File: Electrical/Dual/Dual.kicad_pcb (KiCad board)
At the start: 2 copper layers, 140 x 70 mm, 190 parts, among them J101 01x04, J102 02x04, J103 01x04, J104 01x03, J105 01x03, J106 01x03, J107 01x03, J108 01x03, J109 01x03, J110 01x04, J111 01x04, J112 01x04, J113 01x04, J114 01x03, J115 01x03, J116 01x03, J117 01x03, J201 01x03, J202 01x04, J203 01x03, J204 01x04, J205 01x03, J206 USB_OTG, J207 01x04, J208 01x02, J209 01x04, J210 01x02, J211 01x02, J212 4PostTerm, J213 2PostTerm, J214 2PostTerm, J215 2PostTerm, J216 2PostTerm, J217 2PostTerm, J218 01x02, J219 01x02, Q201 FDC6420C, Q202 FDG1024NZ, Q301 FDC6420C, Q401 FDC6420C, U201 TPD4S012, U202 ACS712ELCTR-05B-T, U203 ACS712ELCTR-05B-T, U204 24LC256, U205 LM2576HVS-ADJ, U206 LM2576HVS-ADJ, x100 02x05, x101 RoutaCell, x102 RoutaCell, x103 RoutaCell, x104 RoutaCell, x105 RoutaCell, x106 RoutaCell, x107 RoutaCell, x108 RoutaCell, x109 RoutaCell, x110 RoutaCell, x111 RoutaCell, x112 RoutaCell, x113 RoutaCell, x114 RoutaCell, x115 RoutaCell, x116 RoutaCell, x117 RoutaCell, x118 RoutaCell, x119 RoutaCell, x120 RoutaCell, x121 RoutaCell, x122 RoutaCell, x123 RoutaCell, x124 RoutaCell, x125 RoutaCell, x126 RoutaCell, x127 RoutaCell, x128 RoutaCell, x129 RoutaCell, x130 RoutaCell, x131 RoutaCell, x132 RoutaCell, x133 RoutaCell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

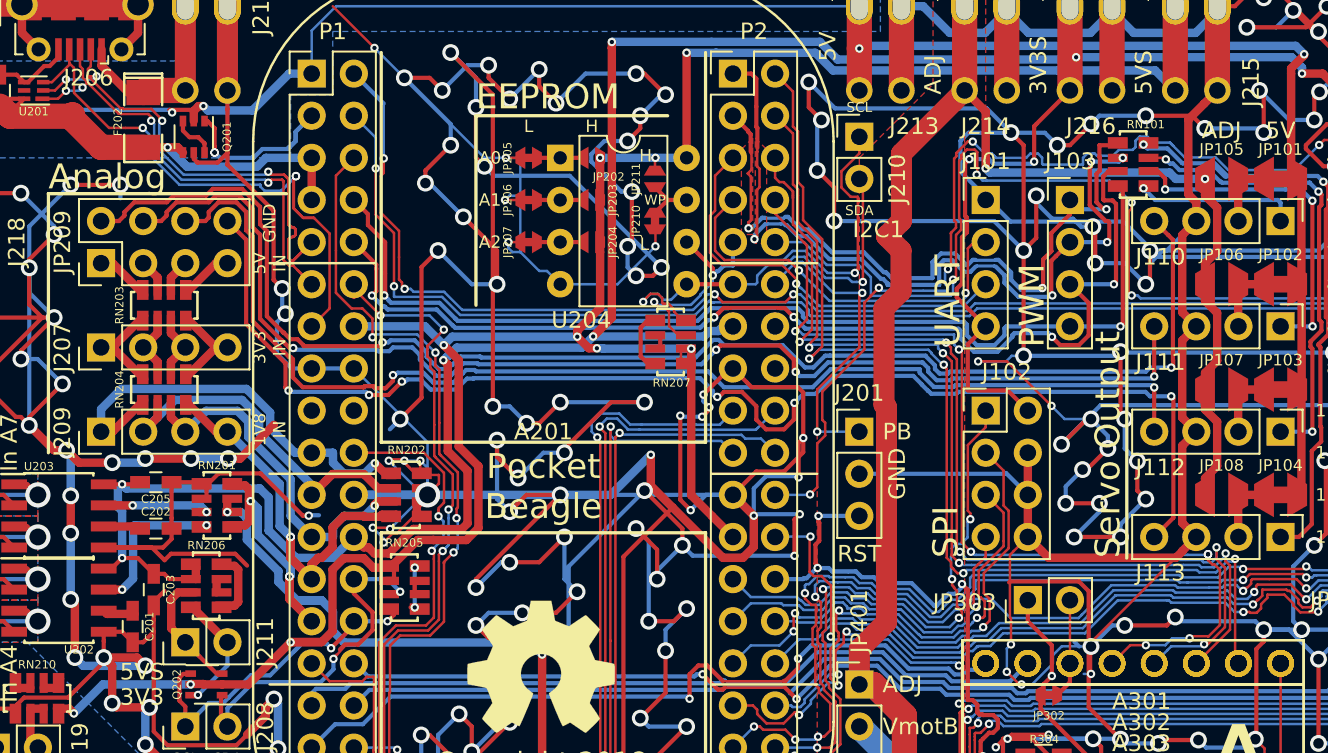
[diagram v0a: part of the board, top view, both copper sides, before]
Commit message: ACS712 -> ACS723
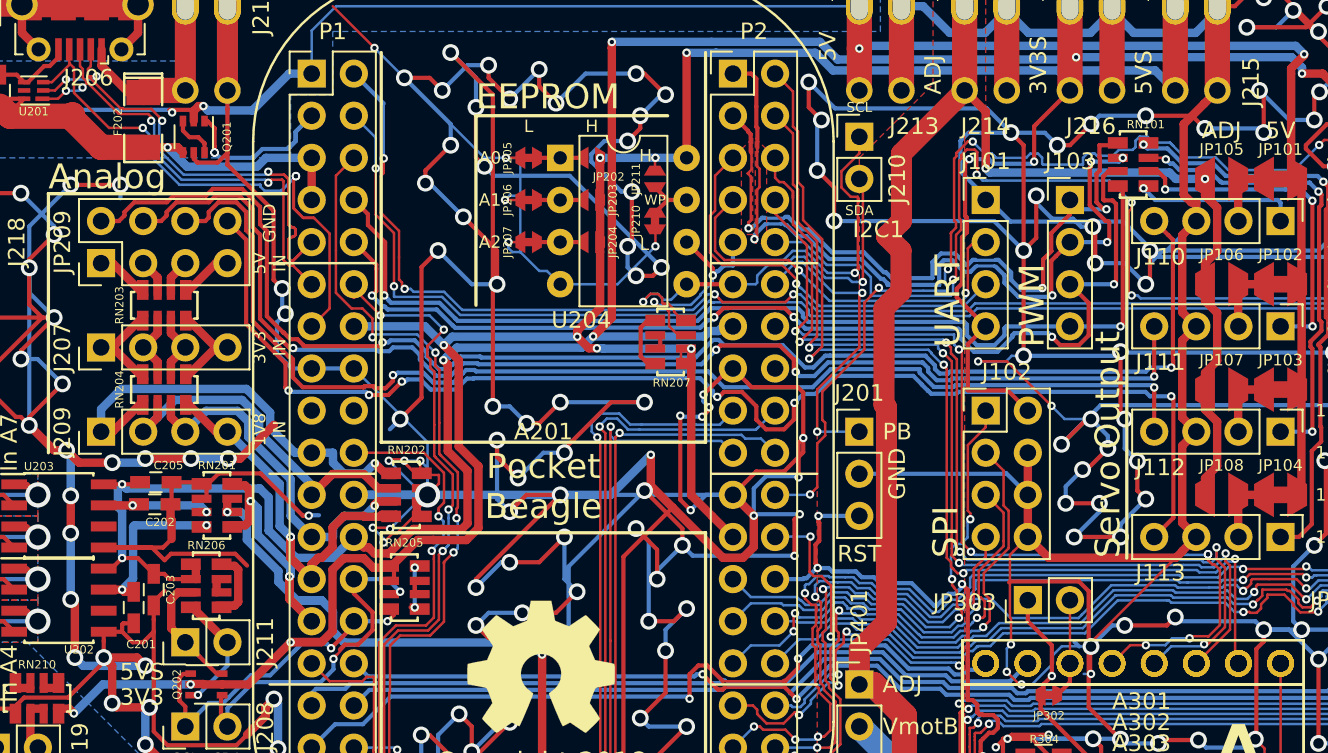
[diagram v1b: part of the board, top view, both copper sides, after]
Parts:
- U202, U203: value ACS712ELCTR-05B-T -> ACS723LLCTR-05AB-T
- moved C202 1.46 mm to (76.6, 96.8)
- moved C201 1.14 mm to (75.3, 103.0)
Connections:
- RN201 pad 7: Net-(RN201-Pad7) -> Net-(C202-Pad1)
- RN201 pad 8: Net-(RN201-Pad8) -> Net-(C201-Pad1)
- U202 pad 6: Net-(C201-Pad1) -> (no net)
- U202 pad 7: Net-(RN201-Pad8) -> Net-(C201-Pad1)
- U203 pad 6: Net-(C202-Pad1) -> (no net)
- U203 pad 7: Net-(RN201-Pad7) -> Net-(C202-Pad1)
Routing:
- net Net-(RN201-Pad8): track 9.64 -> 0.00 mm, vias 2 -> 0
- net Net-(C201-Pad1): track 1.95 -> 10.4 mm, vias 0 -> 2
- net Net-(RN201-Pad7): track 6.81 -> 0.00 mm, vias 2 -> 0
- net Net-(C202-Pad1): track 2.24 -> 7.22 mm, vias 0 -> 2
- net GND: track 2574.8 -> 2578.5 mm

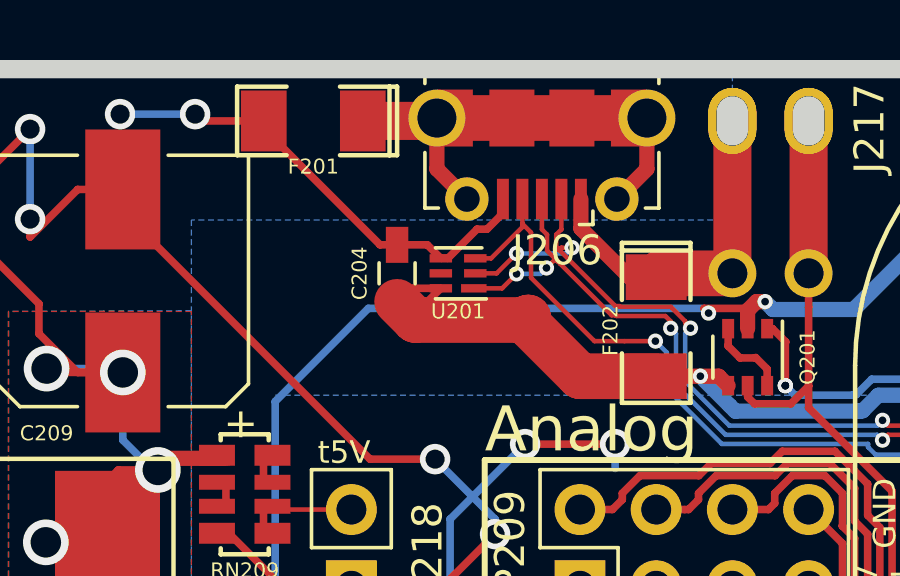
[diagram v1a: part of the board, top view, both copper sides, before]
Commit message: FB <> Fuse; FB == Ferrite Bead
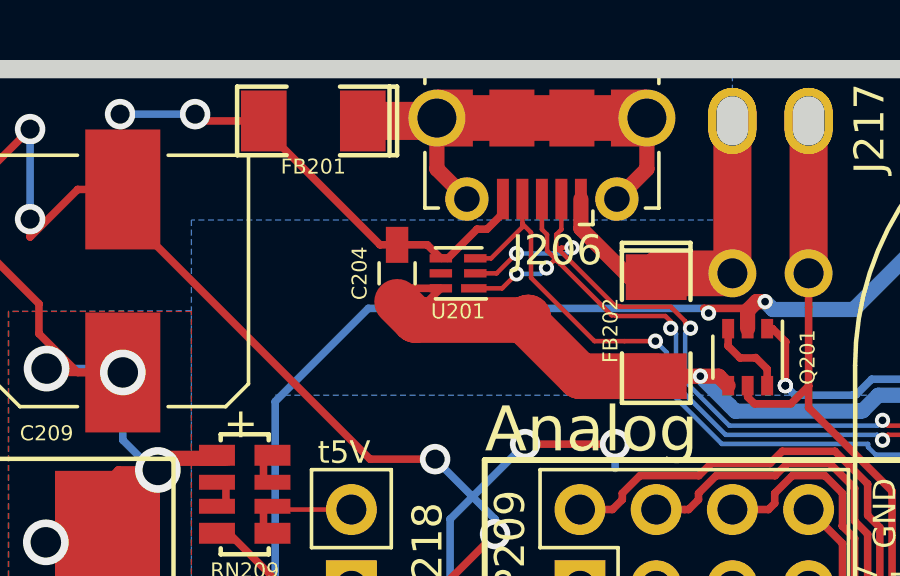
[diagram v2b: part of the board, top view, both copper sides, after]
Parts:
- FB201: renamed from F201; value Fuse -> 120
- FB202: renamed from F202; value Fuse -> 120

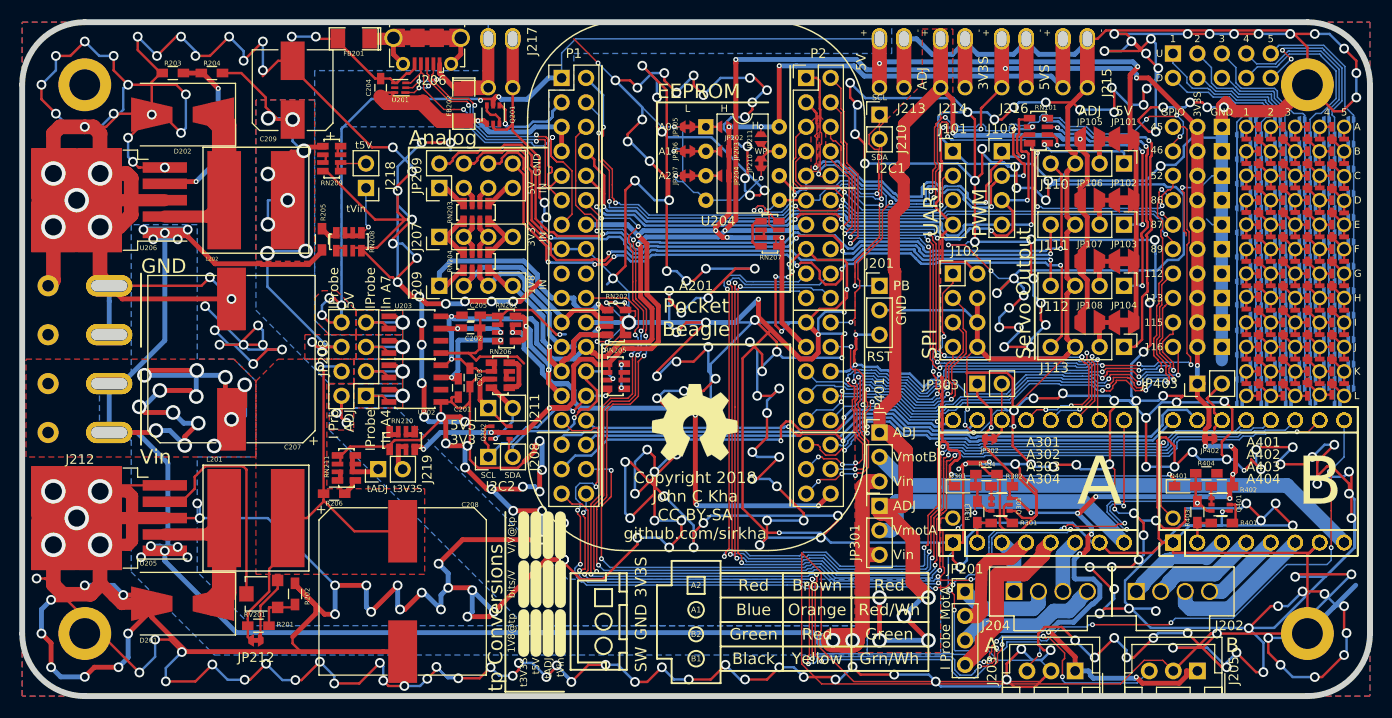
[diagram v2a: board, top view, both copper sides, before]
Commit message: Rearranged the power outputs to support TE Connectivity AMP connectors.
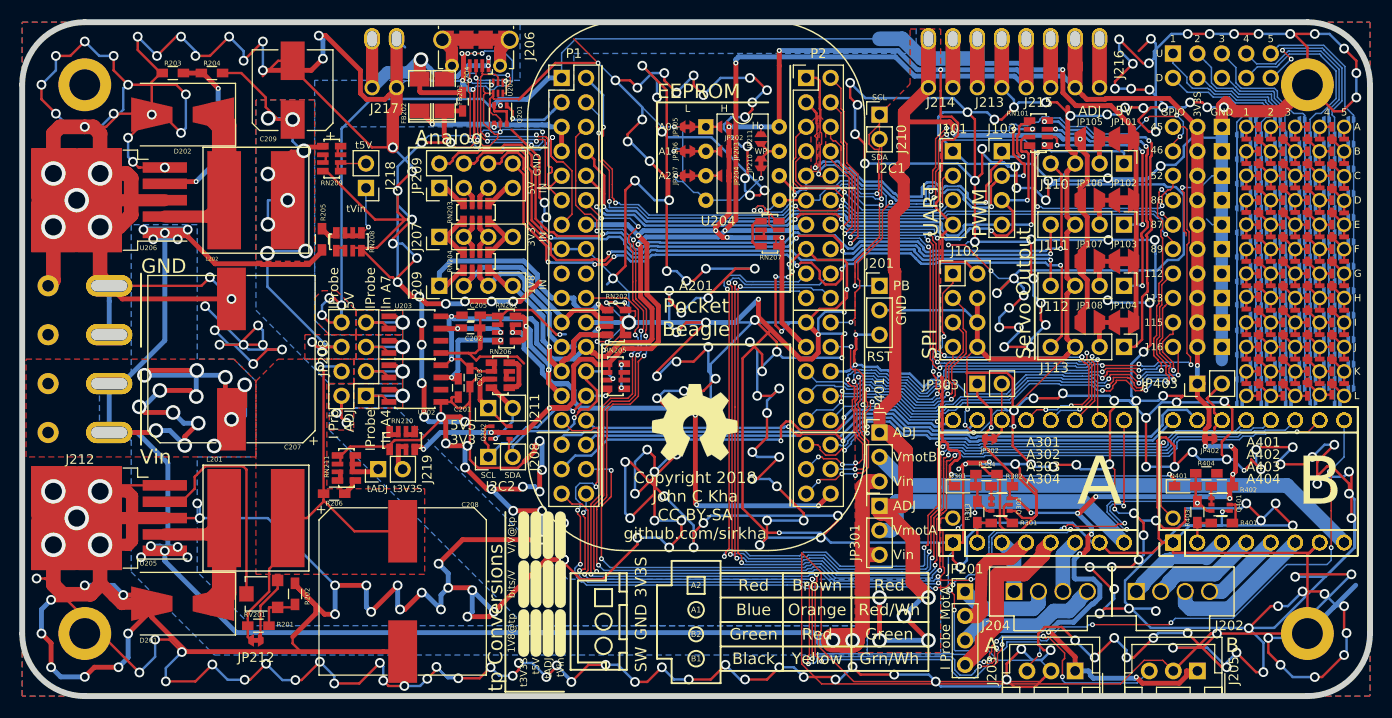
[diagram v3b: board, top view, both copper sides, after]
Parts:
- moved J217 12.1 mm to (67.6, 69.3)
- moved FB201 11.1 mm to (73.8, 72.6), turned to 90 degrees
- moved J213 10.2 mm to (130.5, 69.3)
- moved U201 10.2 mm to (79.4, 71.8), turned to 270 degrees
- moved C204 8.63 mm to (75.7, 73.3), turned to 270 degrees
- moved J216 7.62 mm to (140.6, 69.3)
- moved J206 5.08 mm to (77.1, 67.2)
- moved FB202 4.68 mm to (71.3, 72.6), turned to 90 degrees
- moved J215 3.81 mm to (135.6, 69.3)
- moved J214 1.27 mm to (125.4, 69.3)
- moved Q201 0.76 mm to (79.7, 74.6)
- moved RN101 0.25 mm to (135.6, 76.5)
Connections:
- C204 pad 1: /Common/usb1_vbus -> /Common/usb1_5V
- FB201 pad 1: Net-(FB201-Pad1) -> GND
- FB201 pad 2: GND -> Net-(FB201-Pad2)
- FB202 pad 1: /Common/usb1_5V -> /Common/usb1_vbus
- FB202 pad 2: /Common/usb1_vbus -> /Common/usb1_5V
- J206 pad 6: Net-(FB201-Pad1) -> Net-(FB201-Pad2)
- U201 pad 6: /Common/usb1_vbus -> /Common/usb1_5V
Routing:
- net GND: track 2578.5 -> 2651.5 mm, vias 371 -> 384
- net Net-(FB201-Pad1): track 22.1 -> 0.00 mm
- net /Common/usb1_5V: track 11.8 -> 33.4 mm, vias 0 -> 4
- net Net-(FB201-Pad2): track 0.00 -> 15.0 mm
- net /Common/usb1_vbus: track 27.3 -> 18.9 mm, vias 1 -> 2
- net /Common/usb1_d-: track 36.9 -> 31.9 mm, vias 4 -> 2
- net Vadj: track 137.4 -> 132.7 mm
- net 5VS: track 126.8 -> 123.2 mm
- net /Common/usb1_drvvbus: track 12.3 -> 8.86 mm, vias 2 -> 1
- net /gpio1_20: track 58.2 -> 55.4 mm
- net /gpio1_14: track 63.5 -> 60.8 mm
- net /Common/usb1_d+: track 29.4 -> 26.9 mm
- net /Common/usb1_id: track 37.3 -> 35.8 mm, vias 3 -> 5
- net +5V: track 150.3 -> 149.8 mm, vias 7 -> 5
- net 3V3S: track 322.6 -> 322.3 mm, vias 27 -> 24
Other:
- outline, holes or cut-outs redrawn

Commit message: Modified main power input footprint to support other connectors
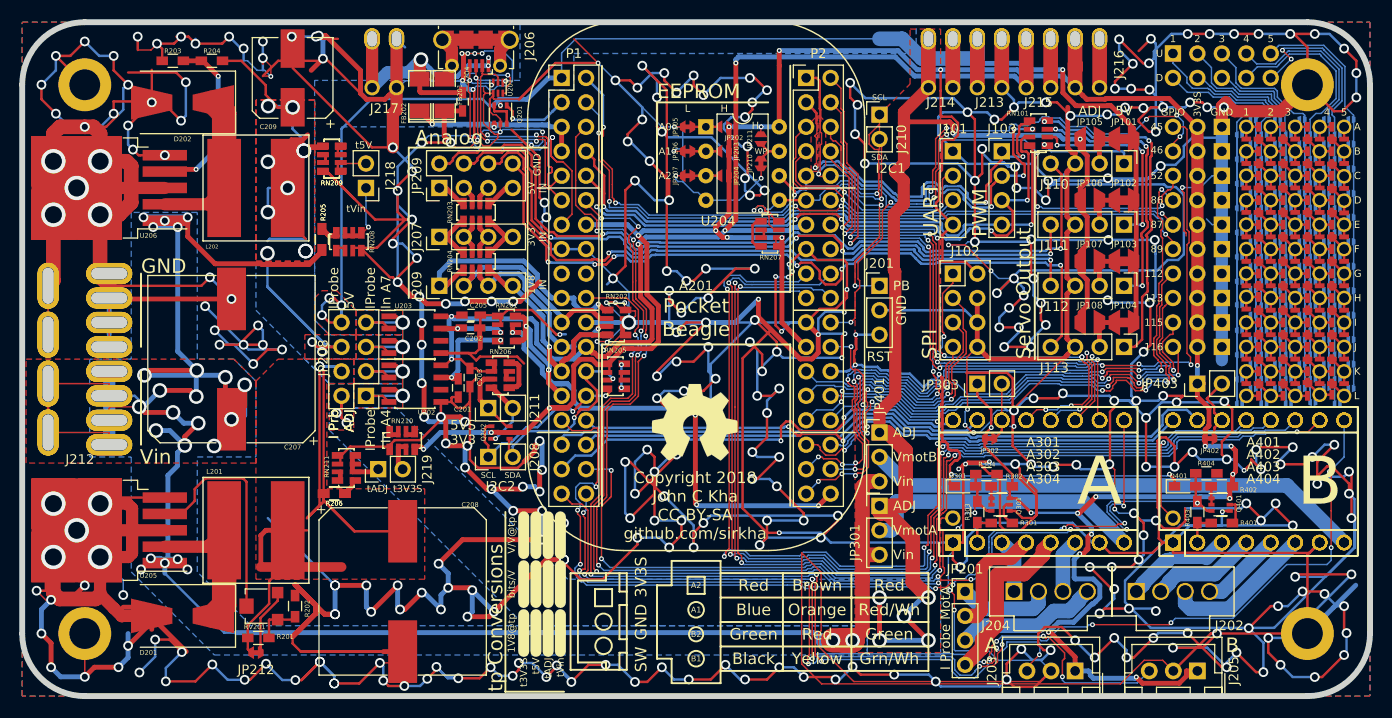
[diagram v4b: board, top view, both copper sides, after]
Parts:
- removed the R205 at (61.1, 87.6)
- removed the R206 at (62.4, 114.0)
- removed the RN209 at (62.2, 79.2)
- added R205 (x2): 12K, Resistors_SMD:R_0603_HandSoldering, F.Cu at (61.1, 87.6)
- added R206 (x2): 12K, Resistors_SMD:R_0603_HandSoldering, F.Cu at (62.4, 114.0)
- added RN209 (x2): 1K2, footprints:R_Array_1206x04, F.Cu at (62.2, 79.2)
- moved C209 1.27 mm to (58.1, 70.8)
- moved D201 1.27 mm to (46.7, 126.7)
- moved D202 1.27 mm to (46.7, 73.3)
- moved L201 1.27 mm to (54.3, 117.8)
- moved L202 1.27 mm to (54.3, 82.2)
- moved R202 1.27 mm to (58.3, 125.7)
- moved R203 1.27 mm to (45.6, 69.0)
- moved R204 1.27 mm to (49.7, 69.0)
- moved RV201 1.27 mm to (54.9, 125.7)
- moved U205 1.27 mm to (39.0, 117.8)
- moved U206 1.27 mm to (39.0, 82.2)
- moved JP212 1.27 mm to (54.3, 130.5)
- moved R201 1.27 mm to (54.5, 129.0)
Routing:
- net /Common/IP_vadj: track 45.2 -> 85.8 mm, vias 1 -> 2
- net Vin: track 246.5 -> 271.1 mm
- net GND: track 2651.5 -> 2668.6 mm, vias 384 -> 389
- net /Common/IP_5V: track 64.0 -> 70.9 mm
- net (no net): track 0.00 -> 4.06 mm, vias 0 -> 2
- net Net-(R205-Pad1): track 1.90 -> 3.79 mm
- net Net-(RN209-Pad2): track 0.80 -> 1.60 mm
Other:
- outline, holes or cut-outs redrawn

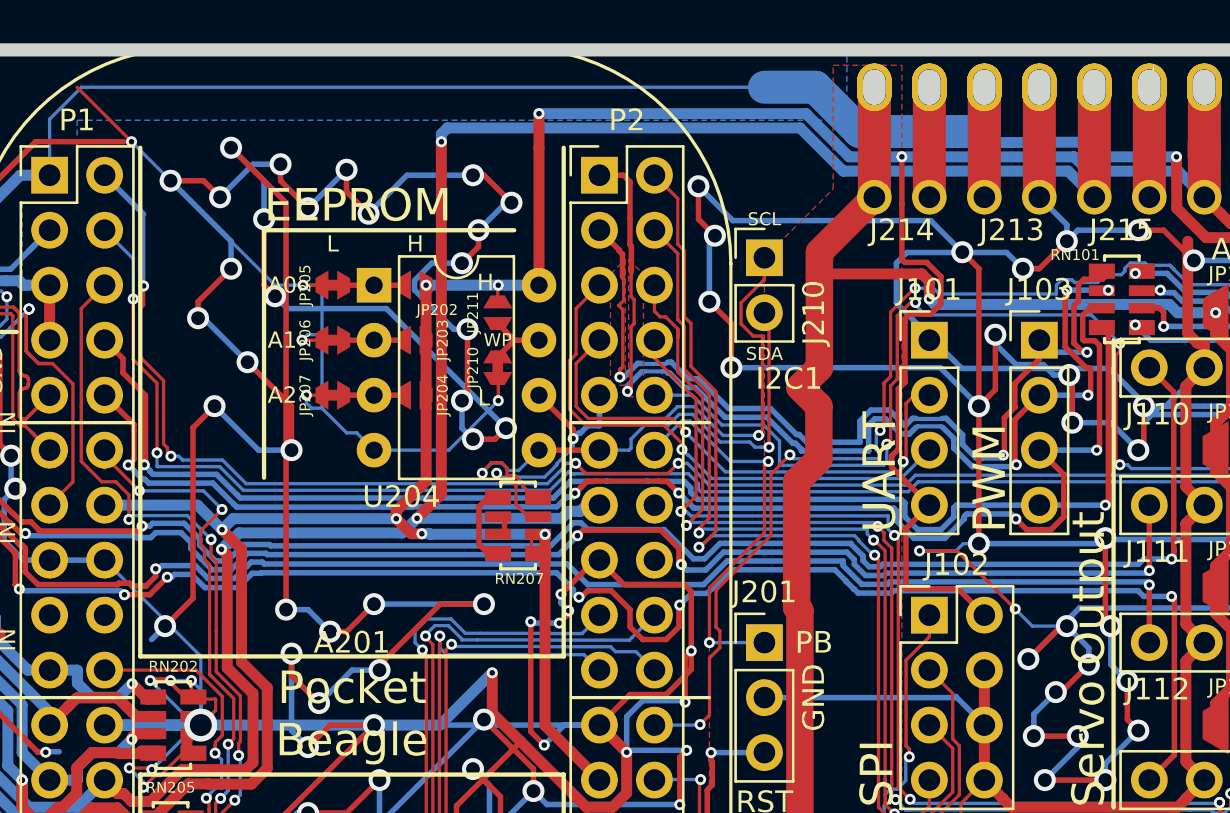
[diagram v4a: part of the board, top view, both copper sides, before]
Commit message: Rearranged EEPROM to add an MSOP option and make the address/WP pins more accessible
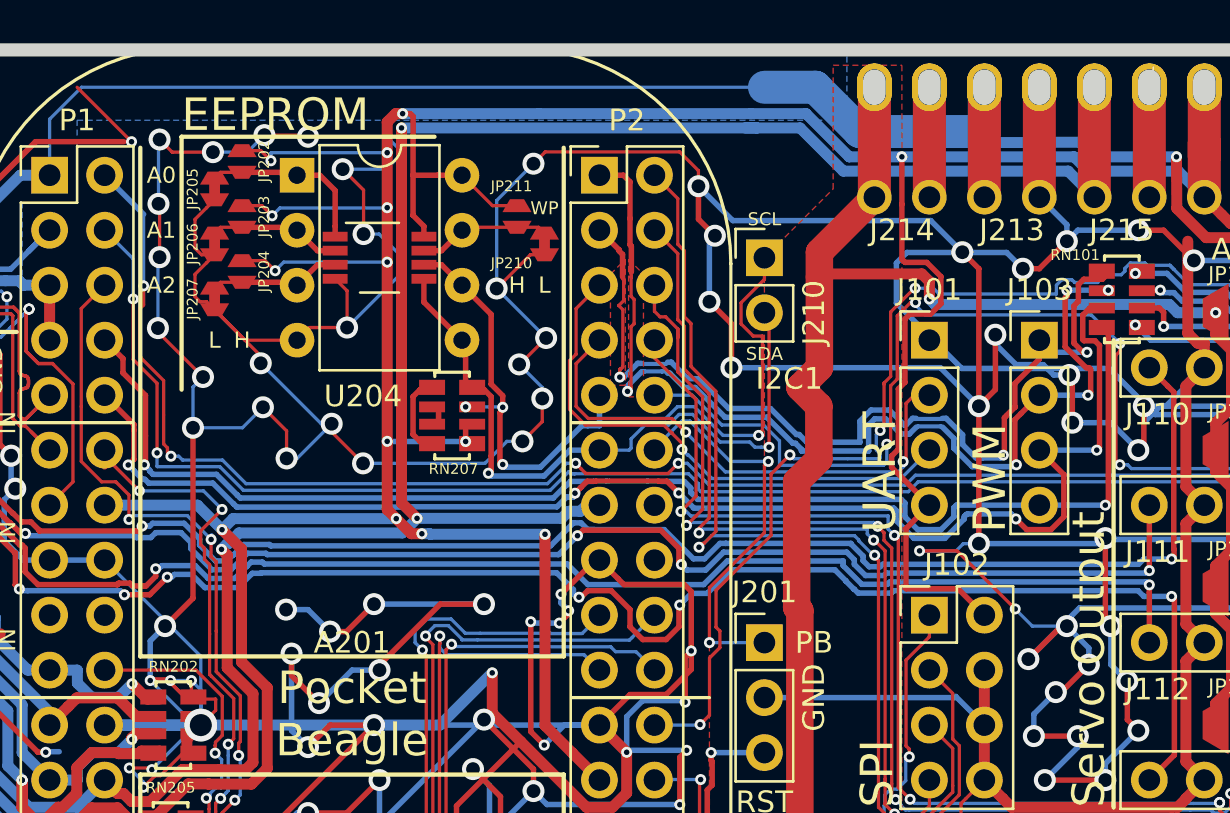
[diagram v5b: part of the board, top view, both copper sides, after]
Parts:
- removed the R205 at (61.1, 87.6) (x2)
- removed the R206 at (62.4, 114.0) (x2)
- removed the RN209 at (62.2, 79.2) (x2)
- added R205 (x2): 12K, Resistors_SMD:R_0603_HandSoldering, F.Cu at (61.1, 87.6)
- added R206 (x2): 12K, Resistors_SMD:R_0603_HandSoldering, F.Cu at (62.4, 114.0)
- added RN209 (x2): 1K2, footprints:R_Array_1206x04, F.Cu at (62.2, 79.2)
- U204: footprint Housings_DIP:DIP-8_W7.62mm -> footprints:Dip-MSOP-8
- moved JP202 9.83 mm to (94.9, 70.2), turned to 270 degrees
- moved JP203 9.83 mm to (94.9, 72.7), turned to 270 degrees
- moved JP204 9.83 mm to (94.9, 75.2), turned to 270 degrees
- moved JP205 7.04 mm to (93.7, 71.4), turned to 90 degrees
- moved JP207 7.04 mm to (93.7, 76.5), turned to 90 degrees
- moved JP206 7.04 mm to (93.7, 74.0), turned to 90 degrees
- moved U204 6.20 mm to (97.5, 70.8)
- moved JP210 6.11 mm to (108.9, 74.0)
- moved RN207 5.92 mm to (104.6, 81.9)
- moved JP211 4.53 mm to (107.6, 72.7)
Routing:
- net 3V3S: track 322.3 -> 359.4 mm, vias 24 -> 30
- net GND: track 2668.6 -> 2644.4 mm, vias 389 -> 386
- net /Common/i2c1_sda: track 25.5 -> 32.2 mm
- net /Common/i2c1_scl: track 30.6 -> 37.3 mm, vias 3 -> 4
- net Net-(JP202-Pad2): track 2.81 -> 8.16 mm
- net Net-(JP203-Pad2): track 2.81 -> 6.13 mm
- net Net-(JP204-Pad2): track 2.81 -> 6.13 mm
- net Net-(JP210-Pad2): track 3.31 -> 6.13 mm
- net 5VS: track 123.2 -> 125.6 mm
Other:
- net class Default: clearance 0.152146 -> 0.14986
- net class Minimum: clearance 0.152146 -> 0.14986
- rule trace_clearance: 0.152146 -> 0.14986
- rule trace_min: 0.152375 -> 0.1524
